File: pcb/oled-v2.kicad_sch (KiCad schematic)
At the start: 26 parts, among them J1 OLED_128x32, U1 MOUDLE-SEEEDUINO-XIAO

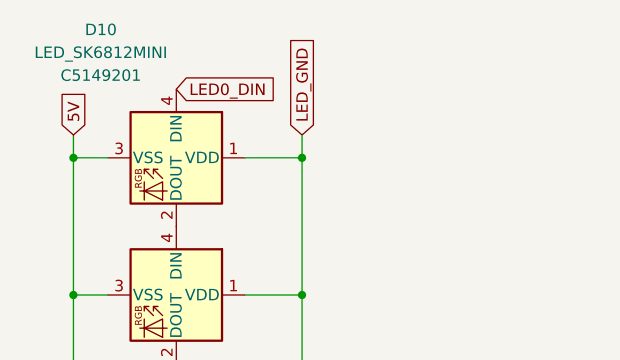
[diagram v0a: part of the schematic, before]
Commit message: turns out I had my GND wired to 5V - fixed now.
production/oled-v2.3mf = full CAD file
images updated
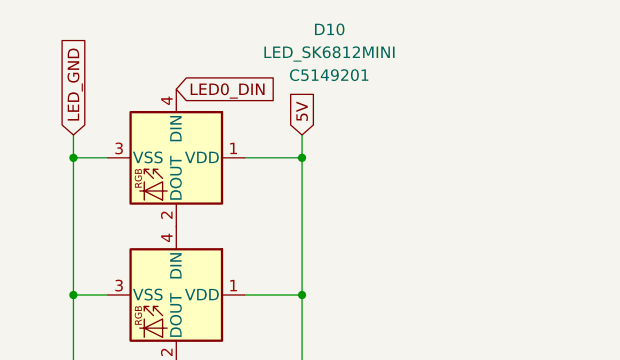
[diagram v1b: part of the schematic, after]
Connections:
- net 5V: now also D10.1 (VDD), D11.1 (VDD), D12.1 (VDD), D13.1 (VDD), D14.1 (VDD), D15.1 (VDD), D16.1 (VDD), D9.1 (VDD); no longer D10.3 (VSS), D11.3 (VSS), D12.3 (VSS), D13.3 (VSS), D14.3 (VSS), D15.3 (VSS), D16.3 (VSS), D9.3 (VSS)
- net GND: now also D10.3 (VSS), D11.3 (VSS), D12.3 (VSS), D13.3 (VSS), D14.3 (VSS), D15.3 (VSS), D16.3 (VSS), D9.3 (VSS); no longer D10.1 (VDD), D11.1 (VDD), D12.1 (VDD), D13.1 (VDD), D14.1 (VDD), D15.1 (VDD), D16.1 (VDD), D9.1 (VDD)
